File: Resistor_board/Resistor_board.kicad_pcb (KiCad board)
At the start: 2 copper layers, 39 x 14 mm, 6 parts, among them J1 Conn_01x06_Pin, SW1 SW_SPDT_312

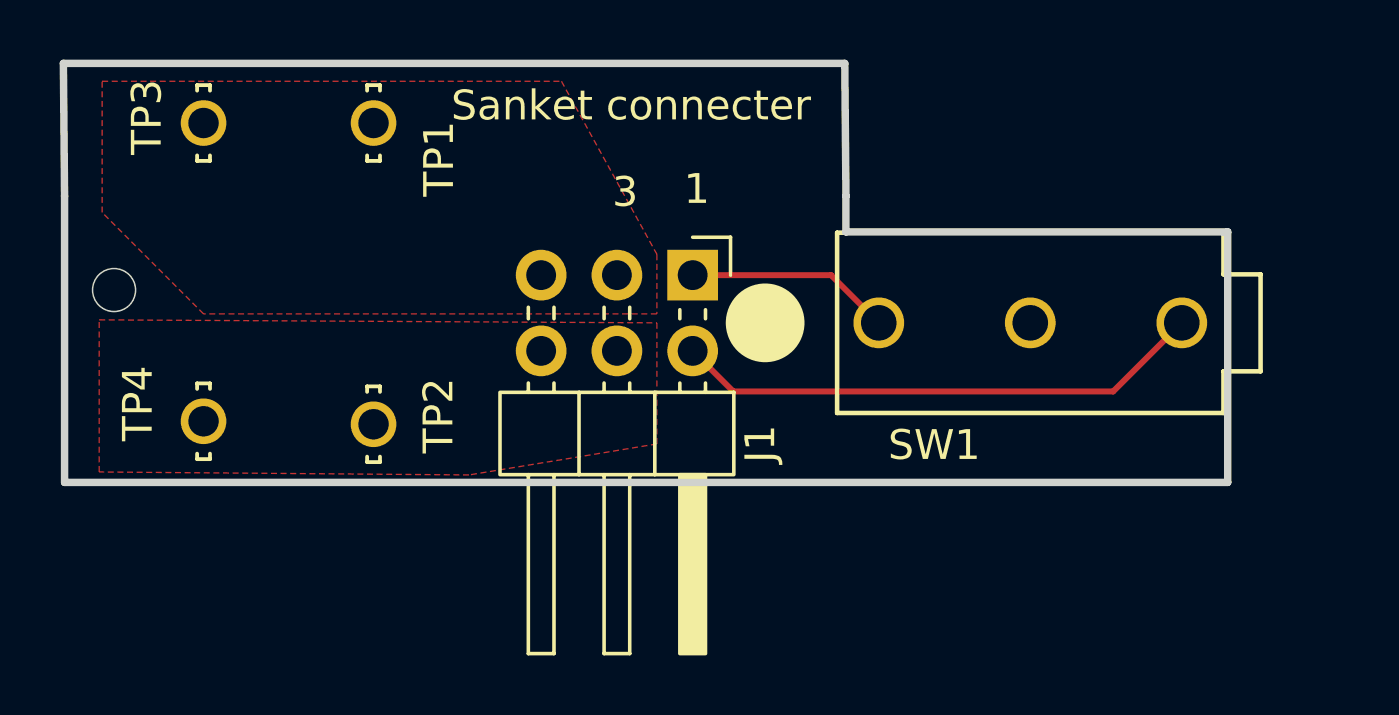
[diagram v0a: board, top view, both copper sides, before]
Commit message: Switch footprint flipped to opposite side, Edgecut layer updated according to new resistor board
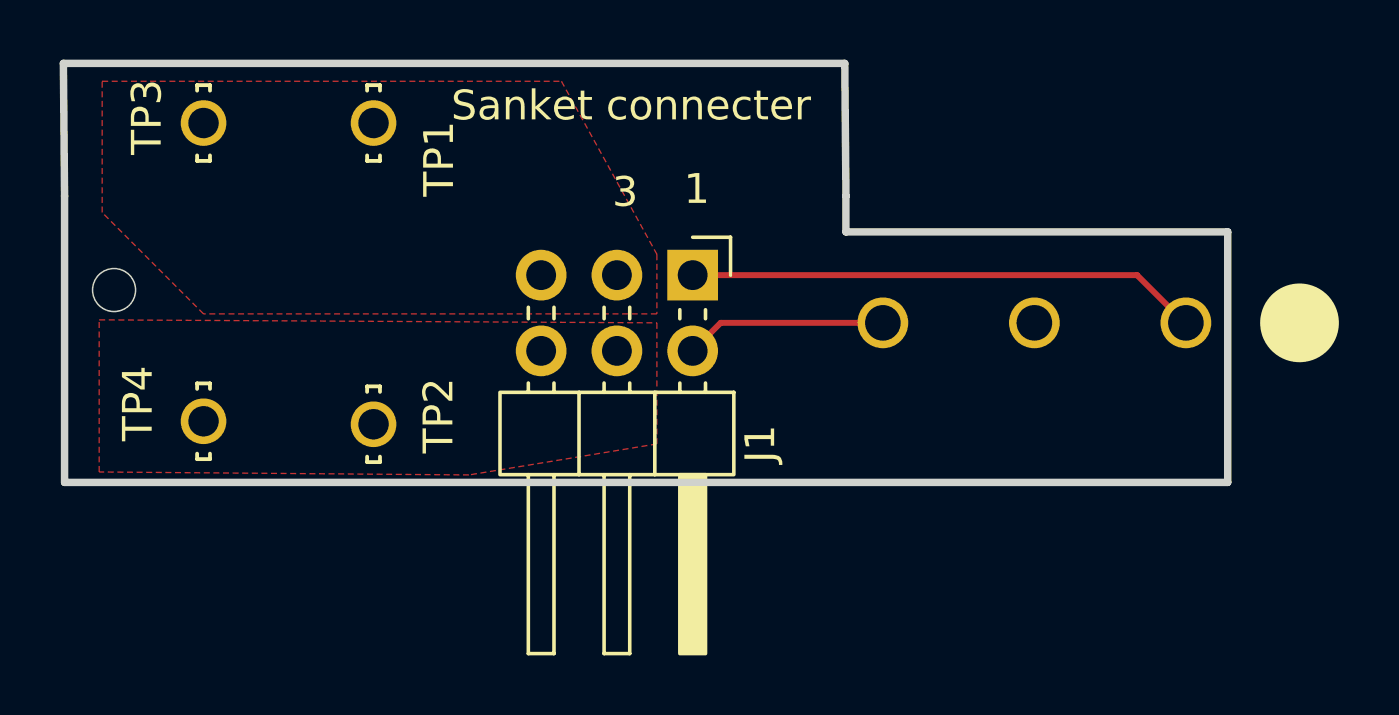
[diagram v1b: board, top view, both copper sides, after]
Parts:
- SW1: moved to B.Cu
- moved SW1 10.3 mm to (147.5, 58.9), turned to 180 degrees
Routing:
- net /DeployerDetectionSWIN: track 17.9 -> 7.10 mm
- net /DeployerDetectionSWOUT: track 7.27 -> 17.2 mm

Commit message: Added missing holw in resistor board, removed NAND gate, added more testpoints
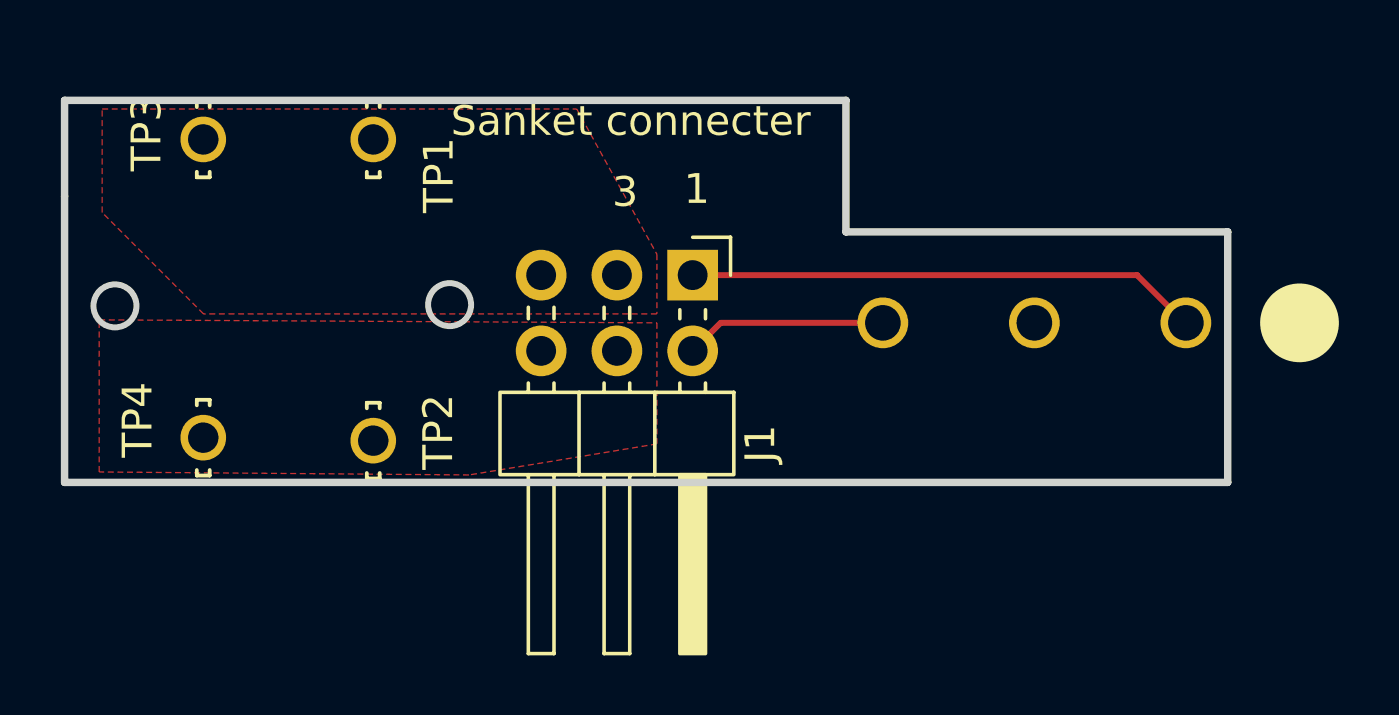
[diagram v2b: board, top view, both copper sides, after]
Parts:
- moved TP2 0.55 mm to (120.3, 62.9)
- moved TP1 0.55 mm to (120.3, 52.8)
- moved TP3 0.55 mm to (114.6, 52.8)
- moved TP4 0.55 mm to (114.6, 62.8)
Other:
- board size 39 x 14 mm -> 39 x 12.8 mm
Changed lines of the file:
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@@
 	(footprint "5021:TP_5021"
 		(layer "F.Cu")
-		(at 114.6 52.2 -90)
+		(at 114.59 52.75 -90)
 		(property "Reference" "TP3"
 			(at -0.2 1.9 90)
@@
 	(footprint "5021:TP_5021"
 		(layer "F.Cu")
-		(at 114.6 62.2 -90)
+		(at 114.59 62.75 -90)
 		(property "Reference" "TP4"
 			(at -0.6 2.2 90)
@@
 	(footprint "5021:TP_5021"
 		(layer "F.Cu")
-		(at 120.3 52.2 -90)
+		(at 120.29 52.75 -90)
 		(property "Reference" "TP1"
 			(at 1.2 -2.2 90)
@@
 	(footprint "5021:TP_5021"
 		(layer "F.Cu")
-		(at 120.3 62.3 -90)
+		(at 120.29 62.85 -90)
 		(property "Reference" "TP2"
 			(at -0.29 -2.18 90)
@@
 	(gr_line
 		(start 109.94 54.65)
-		(end 109.9 50.2)
+		(end 109.94 51.44)
 		(stroke
 			(width 0.25)
@@
 	)
 	(gr_circle
-		(center 111.6 57.8)
-		(end 112.2 58.2)
+		(center 111.63 58.33111)
+		(end 112.23 58.73111)
 		(stroke
-			(width 0.05)
-			(type default)
+			(width 0.2)
+			(type solid)
 		)
 		(fill no)
 		(layer "Edge.Cuts")
 	)
+	(gr_circle
+		(center 122.85 58.28889)
+		(end 123.45 58.68889)
+		(stroke
+			(width 0.2)
+			(type solid)
+		)
+		(fill no)
+		(layer "Edge.Cuts")
+	)
 	(gr_line
-		(start 136.1 50.2)
-		(end 109.9 50.2)
+		(start 136.14 51.44)
+		(end 109.94 51.44)
 		(stroke
 			(width 0.25)
@@
 	)
 	(gr_line
-		(start 136.1 50.2)
-		(end 136.14 54.65)
+		(start 136.14 55.85)
+		(end 136.14 51.44)
 		(stroke
 			(width 0.25)
 			(type solid)
-		)
-		(layer "Edge.Cuts")
-	)
-	(gr_line
-		(start 136.14 55.85)
-		(end 136.14 54.65)
-		(stroke
-			(width 0.25)
-			(type default)
 		)
 		(layer "Edge.Cuts")
@@
 	)
 	(gr_text "Sanket connecter"
-		(at 122.9 52.2 0)
+		(at 122.89 52.72 0)
 		(layer "F.SilkS")
 		(effects
@@
 		(polygon
 			(pts
-				(xy 111.2 50.8) (xy 126.6 50.8) (xy 129.8 56.6) (xy 129.8 58.6) (xy 114.6 58.6) (xy 111.2 55.2)
-			)
-		)
+				(xy 111.2 51.73) (xy 127.113103 51.73) (xy 129.8 56.6) (xy 129.8 58.6) (xy 114.6 58.6) (xy 111.2 55.2)
+			)
+		)
